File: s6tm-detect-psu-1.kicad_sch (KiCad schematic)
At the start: 0 parts

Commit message: schem: add stm32f103c8 mcu
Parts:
- added C10, C11, C12, C14, C6: 0u1, Capacitor_SMD:C_0402_1005Metric, symbol Device:C
- added C15, C16: 1u, Capacitor_SMD:C_0402_1005Metric, symbol Device:C
- added C5: 10u, Capacitor_SMD:C_0805_2012Metric, symbol Device:C
- added C8, C9: 20p, Capacitor_SMD:C_0603_1608Metric, symbol Device:C
- added D7: YELLOW, LED_SMD:LED_0805_2012Metric, symbol Device:LED
- added FB1: 600Ω@100M, Inductor_SMD:L_0805_2012Metric, symbol Device:FerriteBead
- added J5: Conn_01x04_Pin, Connector_PinHeader_2.54mm:PinHeader_1x04_P2.54mm_Vertical, symbol Connector:Conn_01x04_Pin
- added R10: 5k1, Resistor_SMD:R_0402_1005Metric, symbol Device:R
- added R7: 10k, Resistor_SMD:R_0402_1005Metric, symbol Device:R
- added R8: 560, Resistor_SMD:R_0603_1608Metric, symbol Device:R_Small
- added U6: STM32F103C8Tx, Package_QFP:LQFP-48_7x7mm_P0.5mm, symbol MCU_ST_STM32F1:STM32F103C8Tx
- added Y1: 8M, Crystal:Crystal_SMD_5032-2Pin_5.0x3.2mm, symbol Device:Crystal
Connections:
- new net: R10.1, U6.38 (PA15)
- new net: C15.1, FB1.1, U6.9 (VDDA)
- new net: D7.2 (A), R10.2
- new net: C6.2, C8.2, C9.2, R7.1
- new net +3V3: C10.1, C11.1, C12.1, C14.1, C16.1, C5.1, FB1.2, J5.1 (Pin_1), U6.1 (VBAT), U6.24 (VDD), U6.36 (VDD), U6.48 (VDD)
- new net BOOT: R7.2, U6.44 (BOOT0)
- new net CAN_RX: U6.45 (PB8)
- new net CAN_TX: U6.46 (PB9)
- new net GND: C10.2, C11.2, C12.2, C14.2, C15.2, C16.2, C5.2, D7.1 (K), J5.3 (Pin_3), U6.20 (PB2), U6.23 (VSS), U6.35 (VSS), U6.47 (VSS), U6.8 (VSSA)
- new net NRST: C6.1, U6.7 (NRST)
- new net SWCLK: U6.37 (PA14)
- new net SWDIO: U6.34 (PA13)
- new net SWO: U6.39 (PB3)
- new net U0RXD: J5.2 (Pin_2), U6.13 (PA3)
- new net U0TXD: J5.4 (Pin_4), U6.12 (PA2)
- new net XTAL_I: C8.1, U6.5 (PD0), Y1.2
- new net XTAL_O: R8.2, U6.6 (PD1)
- new net XTAL_RO: C9.1, R8.1, Y1.1
- no-connect marks 0 -> 2
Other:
- note added: "CAN Alive"
- note added: "HSE"
- note added: "UART"

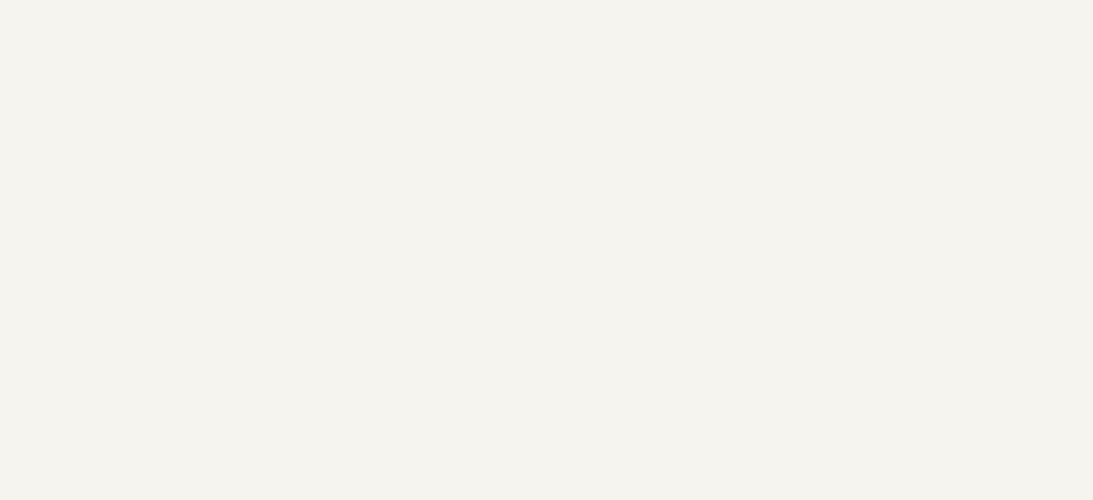
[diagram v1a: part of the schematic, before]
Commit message: schem: add can transceiver and connectors
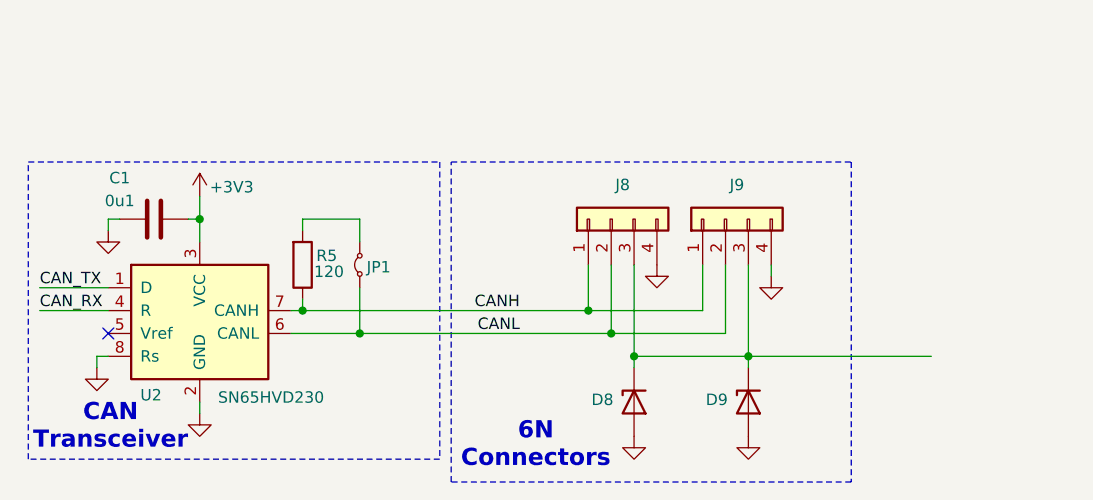
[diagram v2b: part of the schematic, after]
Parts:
- added C1: 0u1, Capacitor_SMD:C_0402_1005Metric, symbol Device:C
- added D8, D9: H5VU10U, GLCS:Diode_DFN1006, symbol GLCS:H5VU10U
- added J8, J9: Conn_01x04, Connector_JST:JST_XH_S4B-XH-A-1_1x04_P2.50mm_Horizontal, symbol Connector_Generic:Conn_01x04
- added JP1: Jumper_2_Small_Bridged, Jumper:SolderJumper-2_P1.3mm_Open_RoundedPad1.0x1.5mm, symbol Jumper:Jumper_2_Small_Bridged
- added R5: 120, Resistor_SMD:R_1206_3216Metric, symbol Device:R
- added U2: SN65HVD230, Package_SO:SOIC-8_3.9x4.9mm_P1.27mm, symbol Interface_CAN_LIN:SN65HVD230
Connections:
- net +3V3: now also C1.1, U2.3 (VCC)
- net CAN_RX: now also U2.4 (R)
- net CAN_TX: now also U2.1 (D)
- net GND: now also C1.2, D8.2 (A), D9.2 (A), J8.4 (Pin_4), J9.4 (Pin_4), U2.2 (GND), U2.8 (Rs)
- new net: JP1.2 (B), R5.2
- new net: D8.1 (K), D9.1 (K), J8.3 (Pin_3), J9.3 (Pin_3)
- new net CANH: J8.1 (Pin_1), J9.1 (Pin_1), R5.1, U2.7 (CANH)
- new net CANL: J8.2 (Pin_2), J9.2 (Pin_2), JP1.1 (A), U2.6 (CANL)
- no-connect marks 2 -> 3
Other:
- note added: "6N Connectors"
- note added: "CAN Transceiver"

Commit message: schem: add boot/rst buttons
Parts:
- added SW1, SW2: SW_Push, Button_Switch_SMD:SW_SPST_TS-1088-xR020, symbol Switch:SW_Push
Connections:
- net +3V3: now also SW1.1
- net BOOT: now also SW1.2
- net GND: now also SW2.1
- net NRST: now also SW2.2
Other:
- note added: "Buttons"

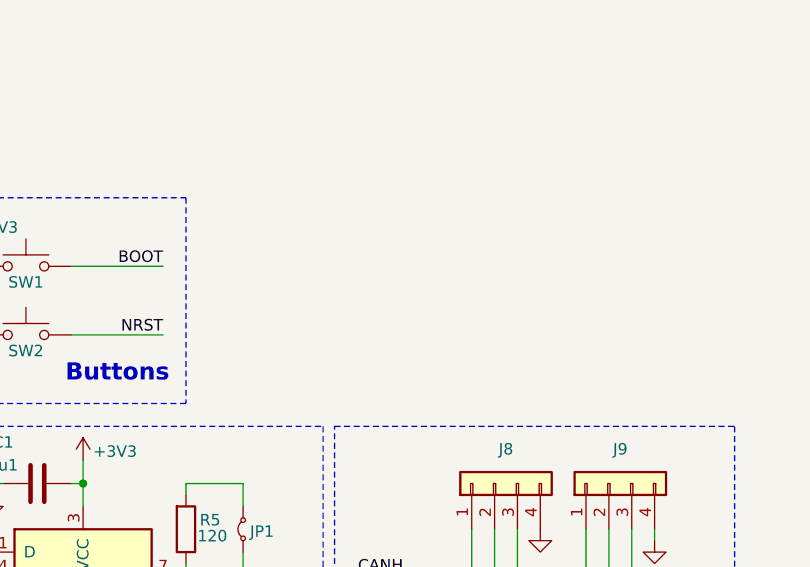
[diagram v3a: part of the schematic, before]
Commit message: schem: add HT753-1 3V3 LDO
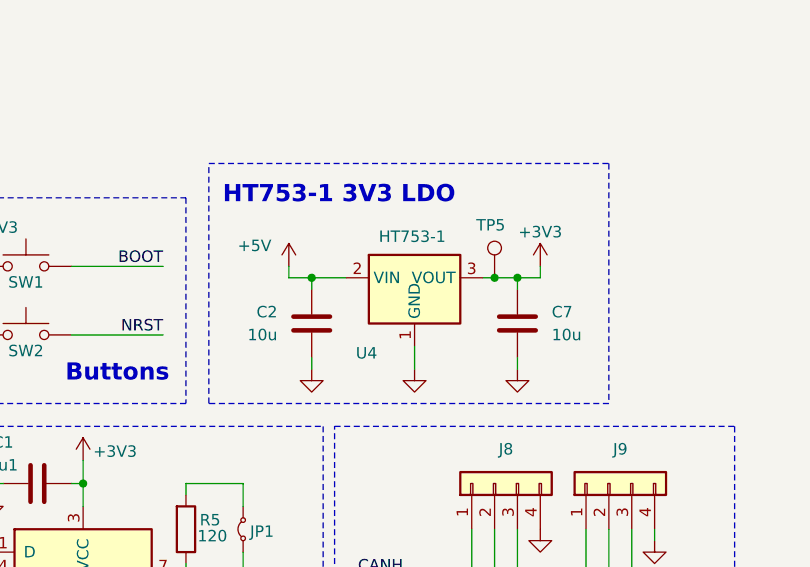
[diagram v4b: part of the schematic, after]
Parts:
- added C2, C7: 10u, Capacitor_SMD:C_0805_2012Metric, symbol Device:C
- added TP5: TestPoint, TestPoint:TestPoint_Pad_D2.0mm, symbol Connector:TestPoint
- added U4: HT753-1, Package_TO_SOT_SMD:SOT-89-3, symbol Regulator_Linear:HT75xx-1-SOT89
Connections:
- net +3V3: now also C7.1, TP5.1, U4.3 (VOUT)
- net GND: now also C2.2, C7.2, U4.1 (GND)
- new net +5V: C2.1, U4.2 (VIN)
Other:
- note added: "HT753-1 3V3 LDO"

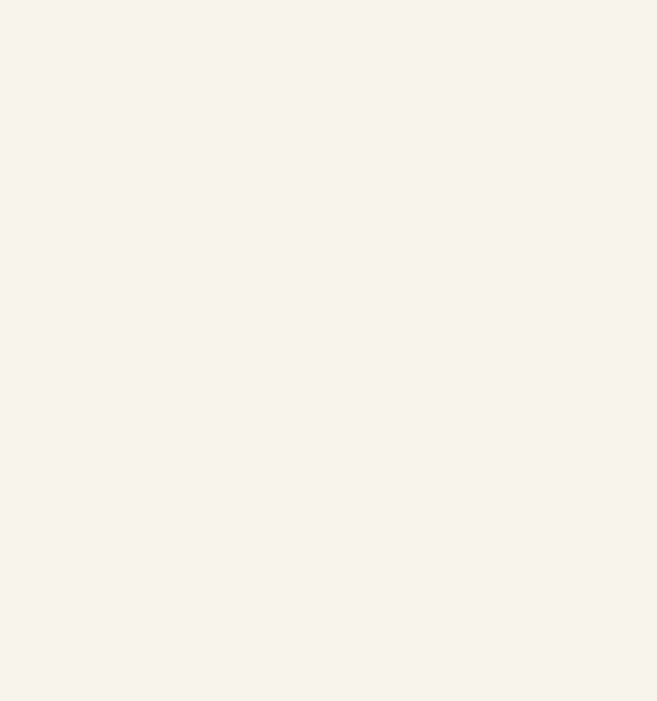
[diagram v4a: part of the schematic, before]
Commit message: schem: add tag connect prog header
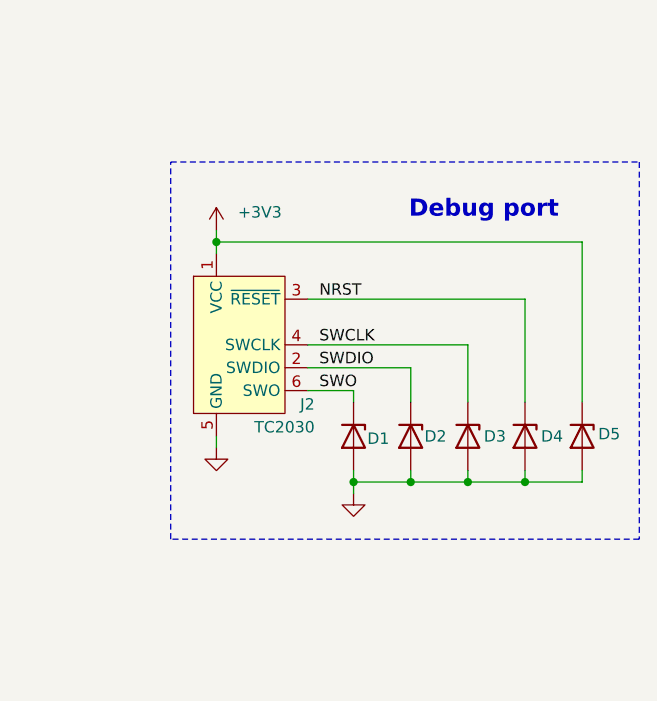
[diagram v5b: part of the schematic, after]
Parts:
- added D1, D2, D3, D4, D5: H5VU10U, GLCS:Diode_DFN1006, symbol GLCS:H5VU10U
- added J2: TC2030, Connector:Tag-Connect_TC2030-IDC-NL_2x03_P1.27mm_Vertical, symbol Connector:Conn_ARM_SWD_TagConnect_TC2030-NL
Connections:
- net +3V3: now also D5.1 (K), J2.1 (VCC)
- net GND: now also D1.2 (A), D2.2 (A), D3.2 (A), D4.2 (A), D5.2 (A), J2.5 (GND)
- net NRST: now also D4.1 (K), J2.3 (~{RESET})
- net SWCLK: now also D3.1 (K), J2.4 (SWCLK)
- net SWDIO: now also D2.1 (K), J2.2 (SWDIO)
- net SWO: now also D1.1 (K), J2.6 (SWO)
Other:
- note added: "Debug port"

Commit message: schem: add +5V pwr
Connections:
- net +5V: now also D8.1 (K), D9.1 (K), J8.3 (Pin_3), J9.3 (Pin_3)
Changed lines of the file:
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@@
 	(wire
 		(pts
+			(xy 104.14 180.34) (xy 104.14 181.61)
+		)
+		(stroke
+			(width 0)
+			(type default)
+		)
+	)
+	(wire
+		(pts
 			(xy 96.52 72.39) (xy 97.79 72.39)
 		)
@@
 	(wire
 		(pts
-			(xy 95.25 181.61) (xy 115.57 181.61)
-		)
-		(stroke
-			(width 0)
-			(type default)
-		)
-	)
-	(wire
-		(pts
 			(xy 33.02 142.24) (xy 43.18 142.24)
 		)
@@
 	(wire
 		(pts
+			(xy 104.14 181.61) (xy 95.25 181.61)
+		)
+		(stroke
+			(width 0)
+			(type default)
+		)
+	)
+	(wire
+		(pts
 			(xy 57.15 142.24) (xy 57.15 143.51)
 		)
@@
 					(unit 1)
 				)
+			)
+		)
+	)
+	(symbol
+		(lib_id "power:+5V")
+		(at 104.14 180.34 0)
+		(unit 1)
+		(body_style 1)
+		(exclude_from_sim no)
+		(in_bom yes)
+		(on_board yes)
+		(in_pos_files yes)
+		(dnp no)
+		(property "Reference" "#PWR018"
+			(at 104.14 184.15 0)
+			(hide yes)
+			(show_name no)
+			(do_not_autoplace no)
+			(effects
+				(font
+					(size 1.27 1.27)
+				)
+			)
+		)
+		(property "Value" "+5V"
+			(at 103.632 176.022 0)
+			(show_name no)
+			(do_not_autoplace no)
+			(effects
+				(font
+					(size 1.27 1.27)
+				)
+			)
+		)
+		(property "Footprint" ""
+			(at 104.14 180.34 0)
+			(hide yes)
+			(show_name no)
+			(do_not_autoplace no)
+			(effects
+				(font
+					(size 1.27 1.27)
+				)
+			)
+		)
+		(property "Datasheet" ""
+			(at 104.14 180.34 0)
+			(hide yes)
+			(show_name no)
+			(do_not_autoplace no)
+			(effects
+				(font
+					(size 1.27 1.27)
+				)
+			)
+		)
+		(property "Description" "Power symbol creates a global label with name \"+5V\""
+			(at 104.14 180.34 0)
+			(hide yes)
+			(show_name no)
+			(do_not_autoplace no)
+			(effects
+				(font
+					(size 1.27 1.27)
+				)
+			)
+		)
+		(pin "1"
+		)
+		(instances
+			(project "s6tm-detect-psu-1"
+				(path "/c28e80f1-f767-484a-bf96-16c1e8738b05"
+					(reference "#PWR018")
+					(unit 1)
+				)

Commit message: schem: add TPS62933P VBAT SMPS
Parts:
- added C13: 0u1, Capacitor_SMD:C_0402_1005Metric, symbol Device:C
- added C18: 0u1, Capacitor_SMD:C_0402_1005Metric, symbol Device:C_Small
- added C19, C20, C21, C3, C4: 10u, Capacitor_SMD:C_0805_2012Metric, symbol Device:C
- added D13: RED, LED_SMD:LED_0805_2012Metric, symbol Device:LED
- added L1: 3u3, Inductor_SMD:L_Sunlord_MWSA0402S, symbol Device:L
- added R11: 52k3, Resistor_SMD:R_0402_1005Metric, symbol Device:R
- added R12: 10k, Resistor_SMD:R_0402_1005Metric, symbol Device:R
- added R36: 5k1, Resistor_SMD:R_0402_1005Metric, symbol Device:R
- added U1: TPS62933, Package_TO_SOT_SMD:SOT-583-8, symbol Regulator_Switching:TPS62933P
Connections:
- net +3V3: now also R36.1
- net GND: now also C13.2, C19.2, C20.2, C21.2, C3.2, C4.2, D13.1 (K), R12.1, U1.1 (RT), U1.4 (GND)
- new net: R11.1, R12.2, U1.8 (FB)
- new net: C18.1, L1.1, U1.5 (SW)
- new net: C18.2, U1.6 (BST)
- new net +5V_SMPS: C19.1, C20.1, C21.1, L1.2, R11.2
- new net +BATT: C13.1, C3.1, C4.1, U1.3 (VIN)
- new net SMPS_PG: D13.2 (A), R36.2, U1.7 (PG)
- no-connect marks 3 -> 4
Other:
- note added: "TPS62933P 5V"

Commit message: schem: add prio 2x 20v battery efuses
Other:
- added sheet 18V efuse (18v-efuse.kicad_sch)
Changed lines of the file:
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@@
+		)
+	)
+	(sheet
+		(at 43.18 101.6)
+		(size 12.7 11.43)
+		(exclude_from_sim no)
+		(in_bom yes)
+		(on_board yes)
+		(dnp no)
+		(fields_autoplaced yes)
+		(stroke
+			(width 0.1524)
+			(type solid)
+		)
+		(fill
+			(color 0 0 0 0)
+		)
+		(property "Sheetname" "18V efuse"
+			(at 43.18 100.8884 0)
+			(show_name no)
+			(do_not_autoplace no)
+			(effects
+				(font
+					(size 1.27 1.27)
+				)
+				(justify left bottom)
+			)
+		)
+		(property "Sheetfile" "18v-efuse.kicad_sch"
+			(at 43.18 113.6146 0)
+			(hide yes)
+			(show_name no)
+			(do_not_autoplace no)
+			(effects
+				(font
+					(size 1.27 1.27)
+				)
+				(justify left top)
+			)
+		)
+		(instances
+			(project "s6tm-detect-psu-1"
+				(path "/c28e80f1-f767-484a-bf96-16c1e8738b05"
+					(page "2")
+				)
+			)
 		)
 	)
